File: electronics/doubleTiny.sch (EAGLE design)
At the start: 15 parts

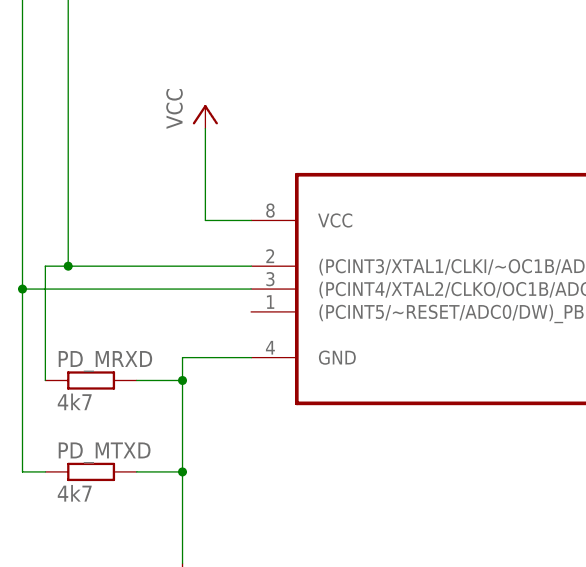
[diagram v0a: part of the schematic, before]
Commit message: updatet schematics and used usbT for capsLock
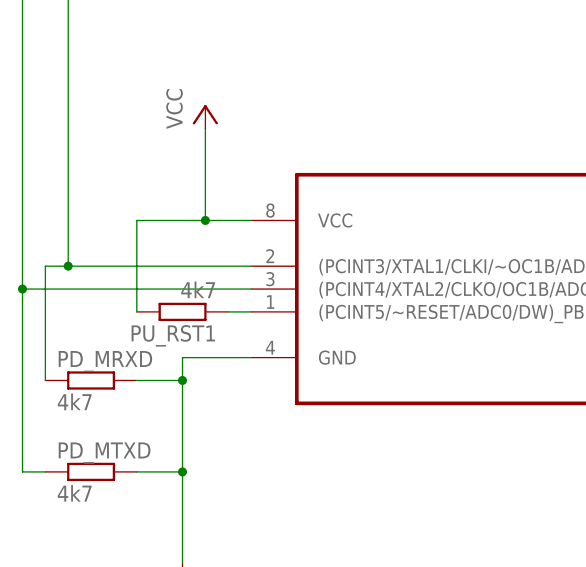
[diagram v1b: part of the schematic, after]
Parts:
- added PU_RST1: 4k7, resistor:R-EU_0309/12
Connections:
- new net N$10: PU_RST1.1, SLAVEAT85.(PCINT5/~RESET/ADC0/DW)_PB5
- net VCC: now also PU_RST1.2
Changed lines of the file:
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@@
 <part name="LED1" library="led" deviceset="LED" device="5MM"/>
 <part name="R_ACTLED" library="resistor" deviceset="R-EU_" device="0309/12" value="330"/>
+<part name="PU_RST1" library="resistor" deviceset="R-EU_" device="0309/12" value="4k7"/>
 </parts>
 <sheets>
@@
 <instance part="LED1" gate="G$1" x="165.1" y="-17.78"/>
 <instance part="R_ACTLED" gate="G$1" x="177.8" y="-25.4"/>
+<instance part="PU_RST1" gate="G$1" x="-12.7" y="-12.7" rot="R180"/>
 </instances>
 <busses>
@@
 <pinref part="SLAVEAT85" gate="A" pin="VCC"/>
 <wire x1="-10.16" y1="-2.54" x2="-5.08" y2="-2.54" width="0.1524" layer="91"/>
+<pinref part="PU_RST1" gate="G$1" pin="2"/>
+<wire x1="-17.78" y1="-12.7" x2="-17.78" y2="-2.54" width="0.1524" layer="91"/>
+<wire x1="-17.78" y1="-2.54" x2="-10.16" y2="-2.54" width="0.1524" layer="91"/>
+<junction x="-10.16" y="-2.54"/>
 </segment>
 <segment>
@@
 </segment>
 </net>
+<net name="N$10" class="0">
+<segment>
+<pinref part="SLAVEAT85" gate="A" pin="(PCINT5/~RESET/ADC0/DW)_PB5"/>
+<pinref part="PU_RST1" gate="G$1" pin="1"/>
+<wire x1="-5.08" y1="-12.7" x2="-7.62" y2="-12.7" width="0.1524" layer="91"/>
+</segment>
+</net>

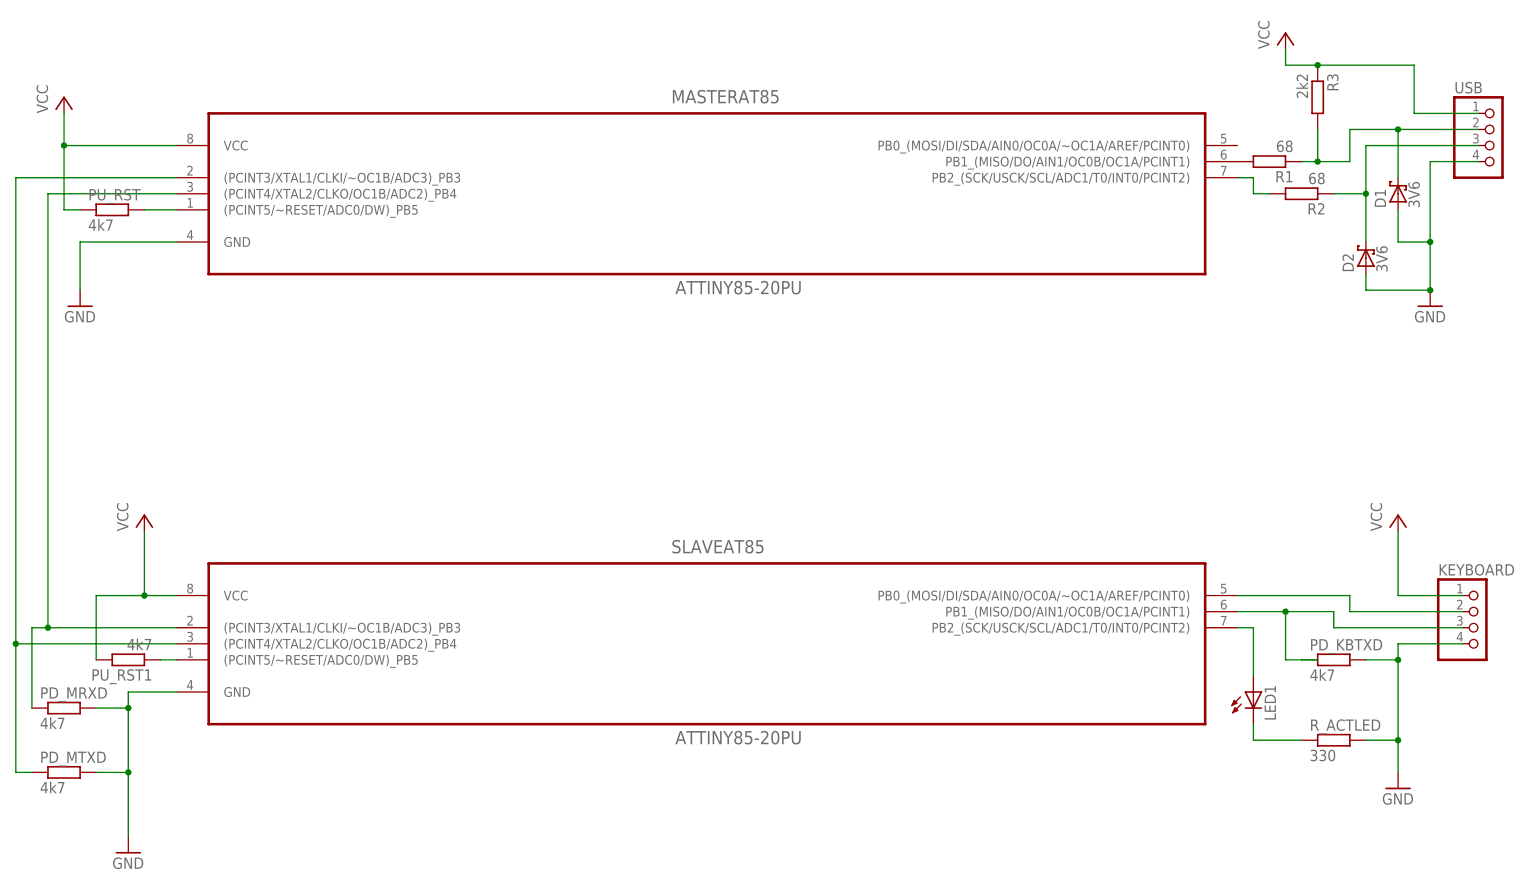
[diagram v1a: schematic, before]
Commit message: created first board layout and added led to master. Swapped usb pins and conglomerated resets
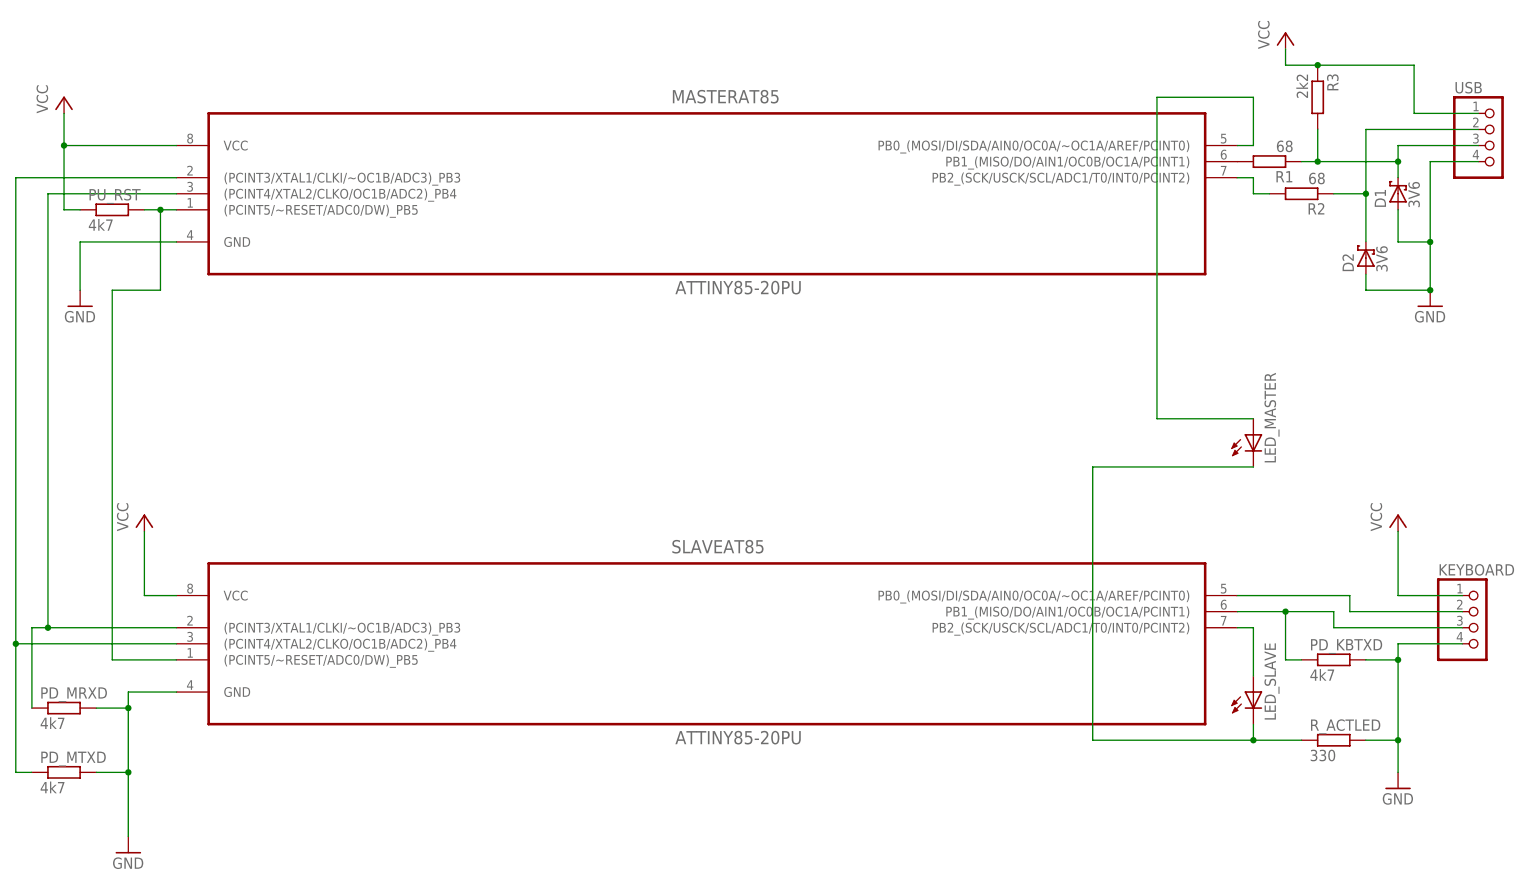
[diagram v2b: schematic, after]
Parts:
- removed PU_RST1: 4k7, resistor:R-EU_0309/12
- added LED_MASTER: (no value), led:LED3MM
- renumbered LED1 to LED_SLAVE
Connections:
- net N$10: now also LED_MASTER.A, MASTERAT85.PB0_(MOSI/DI/SDA/AIN0/OC0A/~OC1A/AREF/PCINT0); no longer PU_RST1.1, SLAVEAT85.(PCINT5/~RESET/ADC0/DW)_PB5
- net N$12: now also LED_MASTER.C
- net N$3: now also USB.3; no longer USB.2
- net N$4: now also USB.2; no longer USB.3
- net N$9: now also SLAVEAT85.(PCINT5/~RESET/ADC0/DW)_PB5
- net VCC: no longer PU_RST1.2
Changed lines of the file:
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@@
 <part name="PD_KBTXD" library="resistor" deviceset="R-EU_" device="0309/12" value="4k7"/>
 <part name="PU_RST" library="resistor" deviceset="R-EU_" device="0309/12" value="4k7"/>
-<part name="LED1" library="led" deviceset="LED" device="5MM"/>
+<part name="LED_SLAVE" library="led" deviceset="LED" device="5MM"/>
 <part name="R_ACTLED" library="resistor" deviceset="R-EU_" device="0309/12" value="330"/>
-<part name="PU_RST1" library="resistor" deviceset="R-EU_" device="0309/12" value="4k7"/>
+<part name="LED_MASTER" library="led" deviceset="LED" device="3MM"/>
 </parts>
 <sheets>
@@
 <instance part="PD_KBTXD" gate="G$1" x="177.8" y="-12.7"/>
 <instance part="PU_RST" gate="G$1" x="-15.24" y="58.42"/>
-<instance part="LED1" gate="G$1" x="165.1" y="-17.78"/>
+<instance part="LED_SLAVE" gate="G$1" x="165.1" y="-17.78"/>
 <instance part="R_ACTLED" gate="G$1" x="177.8" y="-25.4"/>
-<instance part="PU_RST1" gate="G$1" x="-12.7" y="-12.7" rot="R180"/>
+<instance part="LED_MASTER" gate="G$1" x="165.1" y="22.86"/>
 </instances>
 <busses>
@@
 <pinref part="SLAVEAT85" gate="A" pin="VCC"/>
 <wire x1="-10.16" y1="-2.54" x2="-5.08" y2="-2.54" width="0.1524" layer="91"/>
-<pinref part="PU_RST1" gate="G$1" pin="2"/>
-<wire x1="-17.78" y1="-12.7" x2="-17.78" y2="-2.54" width="0.1524" layer="91"/>
-<wire x1="-17.78" y1="-2.54" x2="-10.16" y2="-2.54" width="0.1524" layer="91"/>
-<junction x="-10.16" y="-2.54"/>
 </segment>
 <segment>
@@
 <net name="N$3" class="0">
 <segment>
+<pinref part="D1" gate="1" pin="C"/>
+<wire x1="187.96" y1="63.5" x2="187.96" y2="66.04" width="0.1524" layer="91"/>
+<wire x1="175.26" y1="66.04" x2="187.96" y2="66.04" width="0.1524" layer="91"/>
+<pinref part="R3" gate="G$1" pin="2"/>
+<wire x1="175.26" y1="66.04" x2="175.26" y2="71.12" width="0.1524" layer="91"/>
+<junction x="175.26" y="66.04"/>
 <pinref part="R1" gate="G$1" pin="1"/>
 <wire x1="172.72" y1="66.04" x2="175.26" y2="66.04" width="0.1524" layer="91"/>
-<pinref part="R3" gate="G$1" pin="2"/>
-<wire x1="175.26" y1="66.04" x2="175.26" y2="71.12" width="0.1524" layer="91"/>
-<wire x1="175.26" y1="66.04" x2="180.34" y2="66.04" width="0.1524" layer="91"/>
-<junction x="175.26" y="66.04"/>
-<wire x1="180.34" y1="66.04" x2="180.34" y2="71.12" width="0.1524" layer="91"/>
-<pinref part="USB" gate="A" pin="2"/>
-<wire x1="180.34" y1="71.12" x2="187.96" y2="71.12" width="0.1524" layer="91"/>
-<pinref part="D1" gate="1" pin="C"/>
-<wire x1="187.96" y1="71.12" x2="200.66" y2="71.12" width="0.1524" layer="91"/>
-<wire x1="187.96" y1="63.5" x2="187.96" y2="71.12" width="0.1524" layer="91"/>
-<junction x="187.96" y="71.12"/>
+<pinref part="USB" gate="A" pin="3"/>
+<wire x1="200.66" y1="68.58" x2="187.96" y2="68.58" width="0.1524" layer="91"/>
+<wire x1="187.96" y1="68.58" x2="187.96" y2="66.04" width="0.1524" layer="91"/>
+<junction x="187.96" y="66.04"/>
 </segment>
 </net>
@@
 <pinref part="R2" gate="G$1" pin="1"/>
 <wire x1="177.8" y1="60.96" x2="182.88" y2="60.96" width="0.1524" layer="91"/>
-<wire x1="182.88" y1="60.96" x2="182.88" y2="68.58" width="0.1524" layer="91"/>
-<pinref part="USB" gate="A" pin="3"/>
-<wire x1="182.88" y1="68.58" x2="200.66" y2="68.58" width="0.1524" layer="91"/>
 <pinref part="D2" gate="1" pin="C"/>
 <wire x1="182.88" y1="53.34" x2="182.88" y2="60.96" width="0.1524" layer="91"/>
+<wire x1="182.88" y1="60.96" x2="182.88" y2="71.12" width="0.1524" layer="91"/>
 <junction x="182.88" y="60.96"/>
+<pinref part="USB" gate="A" pin="2"/>
+<wire x1="182.88" y1="71.12" x2="200.66" y2="71.12" width="0.1524" layer="91"/>
 </segment>
 </net>
@@
 <pinref part="KEYBOARD" gate="A" pin="3"/>
 <wire x1="198.12" y1="-7.62" x2="177.8" y2="-7.62" width="0.1524" layer="91"/>
-<pinref part="PD_KBTXD" gate="G$1" pin="1"/>
-<wire x1="172.72" y1="-12.7" x2="170.18" y2="-12.7" width="0.1524" layer="91"/>
 <wire x1="170.18" y1="-12.7" x2="170.18" y2="-5.08" width="0.1524" layer="91"/>
 <junction x="170.18" y="-5.08"/>
-<wire x1="175.26" y1="-12.7" x2="172.72" y2="-12.7" width="0.1524" layer="91"/>
+<pinref part="PD_KBTXD" gate="G$1" pin="1"/>
+<wire x1="170.18" y1="-12.7" x2="172.72" y2="-12.7" width="0.1524" layer="91"/>
 </segment>
 </net>
@@
 <pinref part="PU_RST" gate="G$1" pin="2"/>
 <pinref part="MASTERAT85" gate="A" pin="(PCINT5/~RESET/ADC0/DW)_PB5"/>
-<wire x1="-10.16" y1="58.42" x2="-5.08" y2="58.42" width="0.1524" layer="91"/>
+<wire x1="-10.16" y1="58.42" x2="-7.62" y2="58.42" width="0.1524" layer="91"/>
+<pinref part="SLAVEAT85" gate="A" pin="(PCINT5/~RESET/ADC0/DW)_PB5"/>
+<wire x1="-7.62" y1="58.42" x2="-5.08" y2="58.42" width="0.1524" layer="91"/>
+<wire x1="-5.08" y1="-12.7" x2="-15.24" y2="-12.7" width="0.1524" layer="91"/>
+<wire x1="-15.24" y1="-12.7" x2="-15.24" y2="45.72" width="0.1524" layer="91"/>
+<wire x1="-15.24" y1="45.72" x2="-7.62" y2="45.72" width="0.1524" layer="91"/>
+<wire x1="-7.62" y1="45.72" x2="-7.62" y2="58.42" width="0.1524" layer="91"/>
+<junction x="-7.62" y="58.42"/>
 </segment>
 </net>
@@
 <pinref part="SLAVEAT85" gate="A" pin="PB2_(SCK/USCK/SCL/ADC1/T0/INT0/PCINT2)"/>
 <wire x1="162.56" y1="-7.62" x2="165.1" y2="-7.62" width="0.1524" layer="91"/>
-<pinref part="LED1" gate="G$1" pin="A"/>
+<pinref part="LED_SLAVE" gate="G$1" pin="A"/>
 <wire x1="165.1" y1="-7.62" x2="165.1" y2="-15.24" width="0.1524" layer="91"/>
 </segment>
@@
 <net name="N$12" class="0">
 <segment>
-<pinref part="LED1" gate="G$1" pin="C"/>
+<pinref part="LED_SLAVE" gate="G$1" pin="C"/>
 <wire x1="165.1" y1="-22.86" x2="165.1" y2="-25.4" width="0.1524" layer="91"/>
 <pinref part="R_ACTLED" gate="G$1" pin="1"/>
 <wire x1="165.1" y1="-25.4" x2="172.72" y2="-25.4" width="0.1524" layer="91"/>
+<wire x1="165.1" y1="-25.4" x2="139.7" y2="-25.4" width="0.1524" layer="91"/>
+<wire x1="139.7" y1="-25.4" x2="139.7" y2="17.78" width="0.1524" layer="91"/>
+<junction x="165.1" y="-25.4"/>
+<pinref part="LED_MASTER" gate="G$1" pin="C"/>
+<wire x1="139.7" y1="17.78" x2="165.1" y2="17.78" width="0.1524" layer="91"/>
 </segment>
 </net>
 <net name="N$10" class="0">
 <segment>
-<pinref part="SLAVEAT85" gate="A" pin="(PCINT5/~RESET/ADC0/DW)_PB5"/>
-<pinref part="PU_RST1" gate="G$1" pin="1"/>
-<wire x1="-5.08" y1="-12.7" x2="-7.62" y2="-12.7" width="0.1524" layer="91"/>
-</segment>
-</net>
+<pinref part="LED_MASTER" gate="G$1" pin="A"/>
+<wire x1="165.1" y1="25.4" x2="149.86" y2="25.4" width="0.1524" layer="91"/>
+<wire x1="149.86" y1="25.4" x2="149.86" y2="76.2" width="0.1524" layer="91"/>
+<wire x1="149.86" y1="76.2" x2="165.1" y2="76.2" width="0.1524" layer="91"/>
+<wire x1="165.1" y1="76.2" x2="165.1" y2="68.58" width="0.1524" layer="91"/>
+<pinref part="MASTERAT85" gate="A" pin="PB0_(MOSI/DI/SDA/AIN0/OC0A/~OC1A/AREF/PCINT0)"/>
+<wire x1="165.1" y1="68.58" x2="162.56" y2="68.58" width="0.1524" layer="91"/>
+</segment>
+</net>
